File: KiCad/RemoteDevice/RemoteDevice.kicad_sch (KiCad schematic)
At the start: 55 parts, among them J1 Alim, Q1 Q_PMOS_GSD, Q2 Q_PMOS_GSD, SW1 BP, SW2 BP, U1 XC9140, U10 XBEE-3, U2 STM32L041F6Px, U3 MCP6281, U4 ADT7410TRZ, U5 MCP6281, U6 RT606, U7 Microphone, U8 LD2981CU33, U9 Con_4pts

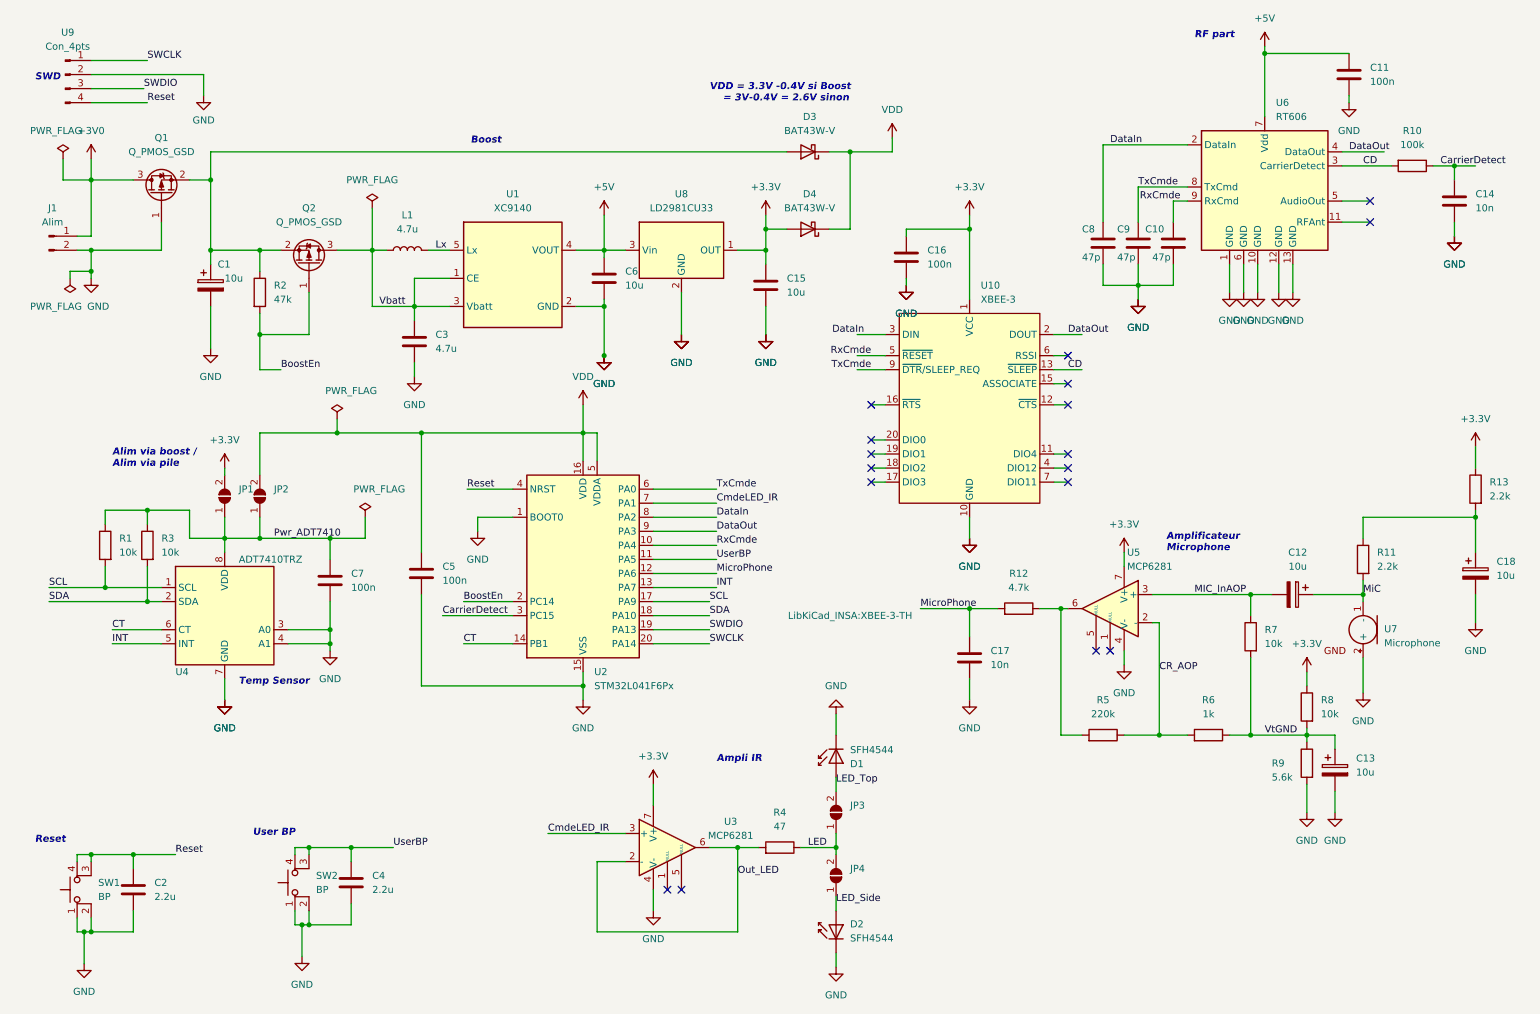
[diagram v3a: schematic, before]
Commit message: Reste la partie Xbee et les résistances de pull up. Bien penser aussi les plans de masse alim...
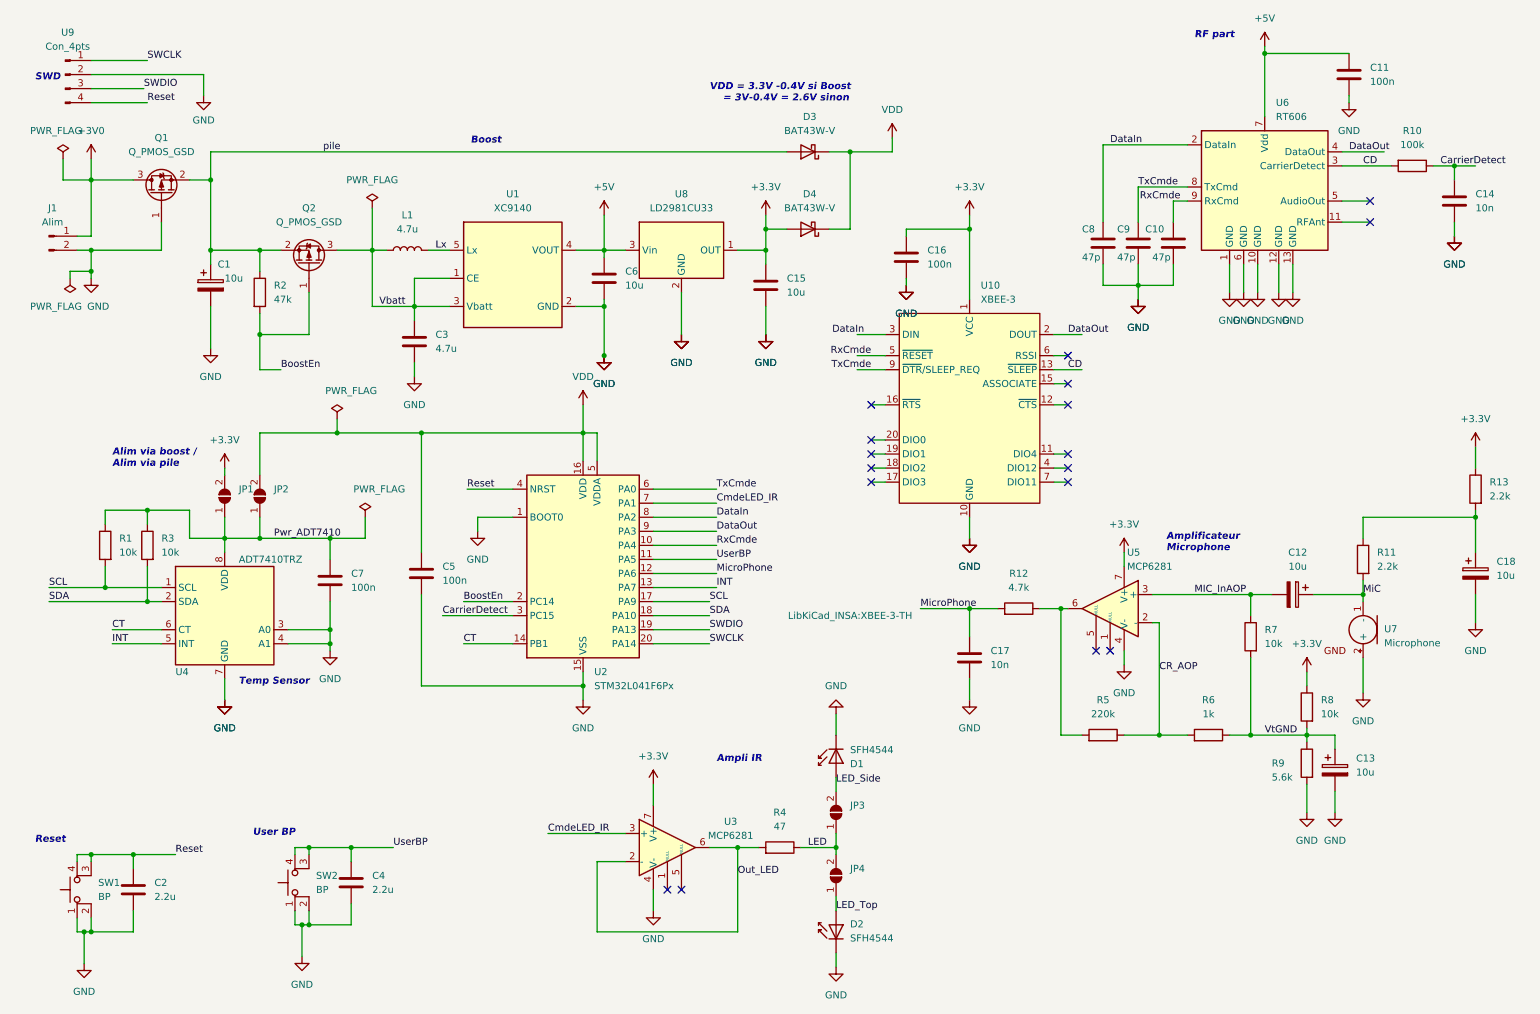
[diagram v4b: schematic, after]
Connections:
- net LED_Side: now also D1.2 (A), JP3.2 (B); no longer D2.2 (A), JP4.1 (A)
- net LED_Top: now also D2.2 (A), JP4.1 (A); no longer D1.2 (A), JP3.2 (B)
- net pile: now reaches C1.1, D3.2 (A), Q1.2 (S), Q2.2 (S), R2.1
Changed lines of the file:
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@@
     (effects (font (size 1.27 1.27)) (justify left bottom))
   )
-  (label "LED_Top" (at 161.29 153.67 0)
+  (label "LED_Top" (at 161.29 176.53 0)
     (effects (font (size 1.27 1.27)) (justify left bottom))
   )
@@
     (effects (font (size 1.27 1.27)) (justify left bottom))
   )
-  (label "LED_Side" (at 161.29 175.26 0)
+  (label "LED_Side" (at 161.29 153.67 0)
     (effects (font (size 1.27 1.27)) (justify left bottom))
   )
@@
     (effects (font (size 1.27 1.27)) (justify left bottom))
   )
+  (label "pile" (at 68.58 39.37 0)
+    (effects (font (size 1.27 1.27)) (justify left bottom))
+  )

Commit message: Routage presque fini, reprendre la partie bottom en niveau de la sériegraphie
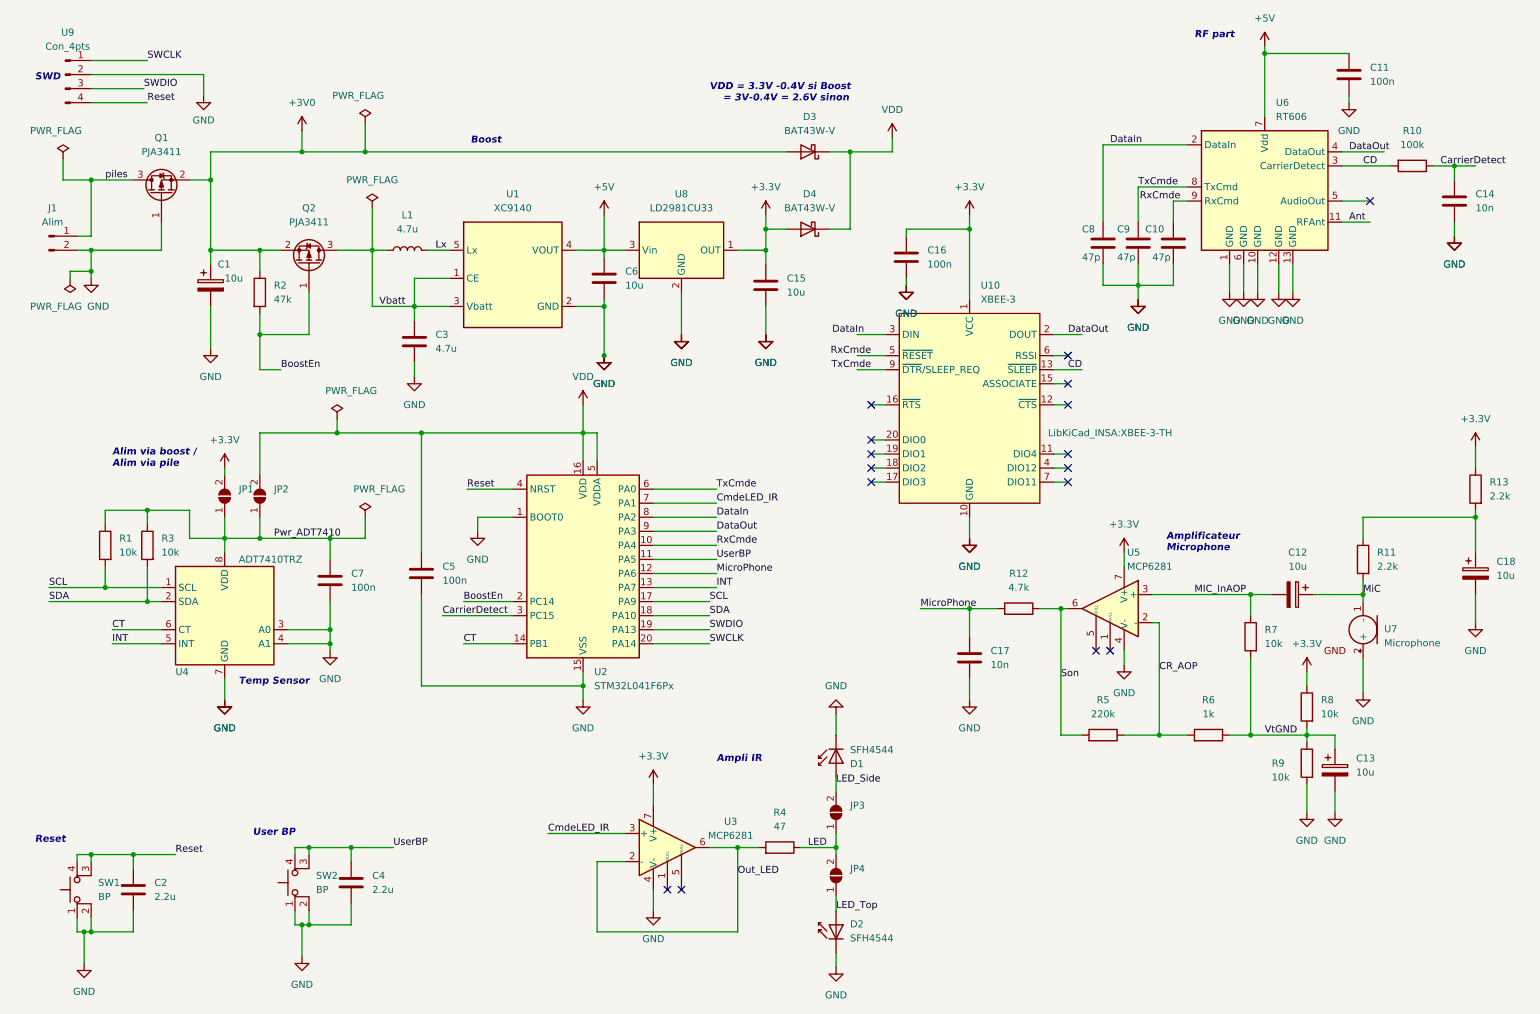
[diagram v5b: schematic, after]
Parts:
- Q1, Q2: value Q_PMOS_GSD -> PJA3411
- R9: value 5.6k -> 10k
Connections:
- net pile is gone; now on net +3V0: C1.1, D3.2 (A), Q1.2 (S), Q2.2 (S), R2.1
- net +3V0: no longer J1.1 (Pin_1), Q1.3 (D)
- net Son: now reaches R12.1, R5.2, U5.6
- net Ant: now reaches U6.11 (RFAnt)
- new net piles: J1.1 (Pin_1), Q1.3 (D)
- no-connect marks 17 -> 16
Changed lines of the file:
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@@
   (junction (at 185.42 121.92) (diameter 0) (color 0 0 0 0)
   )
+  (junction (at 64.77 39.37) (diameter 0) (color 0 0 0 0)
+  )
   (junction (at 215.9 63.5) (diameter 0) (color 0 0 0 0)
   )
@@
   (junction (at 256.54 119.38) (diameter 0) (color 0 0 0 0)
   )
+  (junction (at 76.2 39.37) (diameter 0) (color 0 0 0 0)
+  )
   (junction (at 273.05 41.91) (diameter 0) (color 0 0 0 0)
   )
@@
   )
   (no_connect (at 257.81 48.26))
-  (no_connect (at 257.81 52.07))
   (no_connect (at 210.82 129.54))
   (no_connect (at 208.28 129.54))
@@
     (stroke (width 0) (type default) (color 0 0 0 0))
   )
+  (wire (pts (xy 76.2 34.29) (xy 76.2 39.37))
+    (stroke (width 0) (type default) (color 0 0 0 0))
+  )
   (wire (pts (xy 24.13 177.8) (xy 24.13 180.34))
     (stroke (width 0) (type default) (color 0 0 0 0))
@@
     (stroke (width 0) (type default) (color 0 0 0 0))
   )
+  (wire (pts (xy 64.77 35.56) (xy 64.77 39.37))
+    (stroke (width 0) (type default) (color 0 0 0 0))
+  )
   (wire (pts (xy 238.76 20.32) (xy 238.76 21.59))
     (stroke (width 0) (type default) (color 0 0 0 0))
@@
     (stroke (width 0) (type default) (color 0 0 0 0))
   )
+  (wire (pts (xy 64.77 39.37) (xy 76.2 39.37))
+    (stroke (width 0) (type default) (color 0 0 0 0))
+  )
   (wire (pts (xy 185.42 53.34) (xy 185.42 66.04))
     (stroke (width 0) (type default) (color 0 0 0 0))
@@
     (stroke (width 0) (type default) (color 0 0 0 0))
   )
+  (wire (pts (xy 76.2 39.37) (xy 152.4 39.37))
+    (stroke (width 0) (type default) (color 0 0 0 0))
+  )
   (wire (pts (xy 57.15 90.17) (xy 57.15 97.79))
     (stroke (width 0) (type default) (color 0 0 0 0))
@@
     (stroke (width 0) (type default) (color 0 0 0 0))
   )
+  (wire (pts (xy 128.27 128.27) (xy 138.43 128.27))
+    (stroke (width 0) (type default) (color 0 0 0 0))
+  )
   (wire (pts (xy 252.73 39.37) (xy 260.35 39.37))
     (stroke (width 0) (type default) (color 0 0 0 0))
@@
     (stroke (width 0) (type default) (color 0 0 0 0))
   )
-  (wire (pts (xy 128.27 128.27) (xy 138.43 128.27))
-    (stroke (width 0) (type default) (color 0 0 0 0))
-  )
   (wire (pts (xy 273.05 41.91) (xy 273.05 44.45))
     (stroke (width 0) (type default) (color 0 0 0 0))
@@
     (stroke (width 0) (type default) (color 0 0 0 0))
   )
-  (wire (pts (xy 128.27 125.73) (xy 138.43 125.73))
-    (stroke (width 0) (type default) (color 0 0 0 0))
-  )
   (wire (pts (xy 154.94 165.1) (xy 161.29 165.1))
     (stroke (width 0) (type default) (color 0 0 0 0))
@@
     (stroke (width 0) (type default) (color 0 0 0 0))
   )
-  (wire (pts (xy 48.26 39.37) (xy 152.4 39.37))
+  (wire (pts (xy 48.26 39.37) (xy 64.77 39.37))
     (stroke (width 0) (type default) (color 0 0 0 0))
   )
@@
     (stroke (width 0) (type default) (color 0 0 0 0))
   )
-  (wire (pts (xy 26.67 40.64) (xy 26.67 44.45))
-    (stroke (width 0) (type default) (color 0 0 0 0))
-  )
   (wire (pts (xy 36.83 120.65) (xy 39.37 120.65))
     (stroke (width 0) (type default) (color 0 0 0 0))
@@
     (stroke (width 0) (type default) (color 0 0 0 0))
   )
+  (wire (pts (xy 128.27 125.73) (xy 138.43 125.73))
+    (stroke (width 0) (type default) (color 0 0 0 0))
+  )
   (wire (pts (xy 26.67 166.37) (xy 34.29 166.37))
     (stroke (width 0) (type default) (color 0 0 0 0))
@@
     (effects (font (size 1.27 1.27) bold italic) (justify left bottom))
   )
+  (label "SWDIO" (at 138.43 125.73 0)
+    (effects (font (size 1.27 1.27)) (justify left bottom))
+  )
   (label "CD" (at 203.2 78.74 0)
     (effects (font (size 1.27 1.27)) (justify left bottom))
   )
+  (label "Ant" (at 254 52.07 0)
+    (effects (font (size 1.27 1.27)) (justify left bottom))
+  )
   (label "DataIn" (at 139.7 105.41 0)
     (effects (font (size 1.27 1.27)) (justify left bottom))
@@
     (effects (font (size 1.27 1.27)) (justify left bottom))
   )
-  (label "SWCLK" (at 138.43 128.27 0)
-    (effects (font (size 1.27 1.27)) (justify left bottom))
-  )
   (label "Pwr_ADT7410" (at 59.69 109.22 0)
     (effects (font (size 1.27 1.27)) (justify left bottom))
@@
     (effects (font (size 1.27 1.27)) (justify left bottom))
   )
+  (label "SWCLK" (at 138.43 128.27 0)
+    (effects (font (size 1.27 1.27)) (justify left bottom))
+  )
   (label "RxCmde" (at 223.52 48.26 180)
     (effects (font (size 1.27 1.27)) (justify right bottom))
@@
     (effects (font (size 1.27 1.27)) (justify left bottom))
   )
+  (label "Son" (at 201.93 134.62 0)
+    (effects (font (size 1.27 1.27)) (justify left bottom))
+  )
   (label "CD" (at 256.54 41.91 0)
     (effects (font (size 1.27 1.27)) (justify left bottom))
@@
     (effects (font (size 1.27 1.27)) (justify left bottom))
   )
-  (label "pile" (at 68.58 39.37 0)
+  (label "piles" (at 29.21 44.45 0)
     (effects (font (size 1.27 1.27)) (justify left bottom))
   )
@@
     (effects (font (size 1.27 1.27)) (justify left bottom))
   )
-  (label "SWDIO" (at 138.43 125.73 0)
-    (effects (font (size 1.27 1.27)) (justify left bottom))
-  )
   (label "CT" (at 93.98 128.27 0)
     (effects (font (size 1.27 1.27)) (justify left bottom))
@@
   )
   (symbol (lib_id "Insa:XBEE-3") (at 185.42 105.41 0) (unit 1)
-    (in_bom yes) (on_board yes) (fields_autoplaced)
+    (in_bom yes) (on_board yes)
     (property "Reference" "U10" (id 0) (at 187.4394 63.5 0)
       (effects (font (size 1.27 1.27)) (justify left))
@@
       (effects (font (size 1.27 1.27)) (justify left))
     )
-    (property "Footprint" "LibKiCad_INSA:XBEE-3-TH" (id 2) (at 163.83 123.19 0))
+    (property "Footprint" "LibKiCad_INSA:XBEE-3-TH" (id 2) (at 210.82 90.17 0))
     (property "Datasheet" "" (id 3) (at 163.83 123.19 0)
       (effects (font (size 1.27 1.27)) hide)
@@
     (in_bom yes) (on_board yes) (fields_autoplaced)
     (property "Reference" "Q1" (id 0) (at 39.37 36.83 90))
-    (property "Value" "Q_PMOS_GSD" (id 1) (at 39.37 39.37 90))
+    (property "Value" "PJA3411" (id 1) (at 39.37 39.37 90))
     (property "Footprint" "Package_TO_SOT_SMD:SOT-23" (id 2) (at 36.83 41.91 0)
       (effects (font (size 1.27 1.27)) hide)
@@
     (pin "1")
   )
-  (symbol (lib_id "power:+3V0") (at 26.67 40.64 0) (unit 1)
+  (symbol (lib_id "power:+3V0") (at 64.77 35.56 0) (unit 1)
     (in_bom yes) (on_board yes) (fields_autoplaced)
-    (property "Reference" "#PWR01" (id 0) (at 26.67 44.45 0)
+    (property "Reference" "#PWR01" (id 0) (at 64.77 39.37 0)
       (effects (font (size 1.27 1.27)) hide)
     )
-    (property "Value" "+3V0" (id 1) (at 26.67 35.56 0))
-    (property "Footprint" "" (id 2) (at 26.67 40.64 0)
+    (property "Value" "+3V0" (id 1) (at 64.77 30.48 0))
+    (property "Footprint" "" (id 2) (at 64.77 35.56 0)
       (effects (font (size 1.27 1.27)) hide)
     )
-    (property "Datasheet" "" (id 3) (at 26.67 40.64 0)
+    (property "Datasheet" "" (id 3) (at 64.77 35.56 0)
       (effects (font (size 1.27 1.27)) hide)
     )
@@
       (effects (font (size 1.27 1.27)) (justify right))
     )
-    (property "Value" "5.6k" (id 1) (at 240.03 152.4 0)
+    (property "Value" "10k" (id 1) (at 240.03 152.4 0)
       (effects (font (size 1.27 1.27)) (justify right))
     )
@@
     (pin "1")
   )
+  (symbol (lib_id "power:PWR_FLAG") (at 76.2 34.29 0) (unit 1)
+    (in_bom yes) (on_board yes)
+    (property "Reference" "#FLG0103" (id 0) (at 76.2 32.385 0)
+      (effects (font (size 1.27 1.27)) hide)
+    )
+    (property "Value" "PWR_FLAG" (id 1) (at 74.93 29.21 0))
+    (property "Footprint" "" (id 2) (at 76.2 34.29 0)
+      (effects (font (size 1.27 1.27)) hide)
+    )
+    (property "Datasheet" "~" (id 3) (at 76.2 34.29 0)
+      (effects (font (size 1.27 1.27)) hide)
+    )
+    (pin "1")
+  )
   (symbol (lib_id "power:GND") (at 173.99 63.5 0) (unit 1)
     (in_bom yes) (on_board yes) (fields_autoplaced)
@@
     (in_bom yes) (on_board yes) (fields_autoplaced)
     (property "Reference" "Q2" (id 0) (at 66.04 49.53 90))
-    (property "Value" "Q_PMOS_GSD" (id 1) (at 66.04 52.07 90))
+    (property "Value" "PJA3411" (id 1) (at 66.04 52.07 90))
     (property "Footprint" "Package_TO_SOT_SMD:SOT-23" (id 2) (at 68.58 54.61 0)
       (effects (font (size 1.27 1.27)) hide)
@@
       (reference "#FLG0102") (unit 1) (value "PWR_FLAG") (footprint "")
     )
+    (path "/69a1fce9-6bf3-4cf6-bb72-03bd20828044"
+      (reference "#FLG0103") (unit 1) (value "PWR_FLAG") (footprint "")
+    )
     (path "/5e2d6ecd-63d6-494b-a588-676d49c01485"
       (reference "#PWR01") (unit 1) (value "+3V0") (footprint "")
@@
     )
     (path "/309ab532-fbfc-4b78-b9be-dd62da22f1c1"
-      (reference "Q1") (unit 1) (value "Q_PMOS_GSD") (footprint "Package_TO_SOT_SMD:SOT-23")
+      (reference "Q1") (unit 1) (value "PJA3411") (footprint "Package_TO_SOT_SMD:SOT-23")
     )
     (path "/70d76e55-908c-4803-85fa-52541360684c"
-      (reference "Q2") (unit 1) (value "Q_PMOS_GSD") (footprint "Package_TO_SOT_SMD:SOT-23")
+      (reference "Q2") (unit 1) (value "PJA3411") (footprint "Package_TO_SOT_SMD:SOT-23")
     )
     (path "/64237b66-5629-4cfd-865f-19c8e3222e7e"
@@
     )
     (path "/632c35d8-3649-4945-96ab-c540811010a8"
-      (reference "R9") (unit 1) (value "5.6k") (footprint "Resistor_SMD:R_1206_3216Metric")
+      (reference "R9") (unit 1) (value "10k") (footprint "Resistor_SMD:R_1206_3216Metric")
     )
     (path "/d46aace0-661d-49a9-9148-e3b2e1caa4bf"
